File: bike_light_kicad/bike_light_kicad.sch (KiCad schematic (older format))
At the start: 58 parts, among them J1 12401832E402A, J2 AVR-ISP-6, SW1 SW_SPST, SW2 SW_SPST, U1 BQ29700, U2 bq21040, U3 CSD16406Q3, U4 CSD16406Q3, U5 ATtiny85-20SU, U6 LM2621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

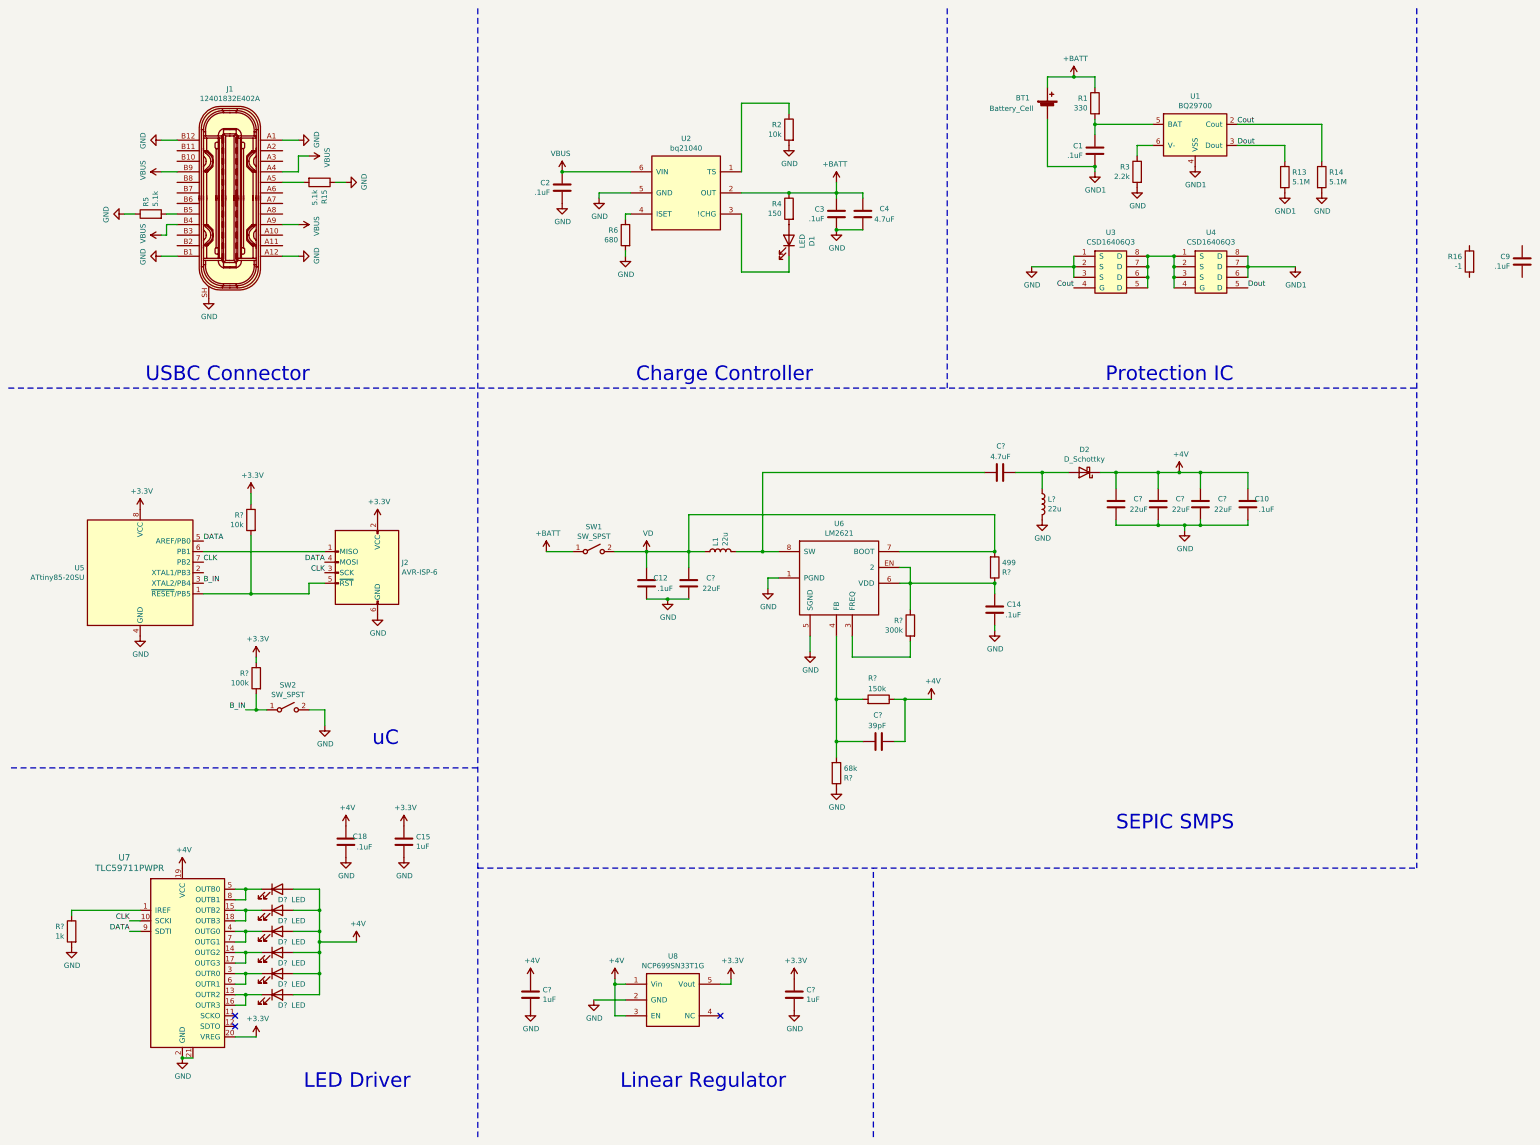
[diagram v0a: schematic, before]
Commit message: Footprints added, new manual lib
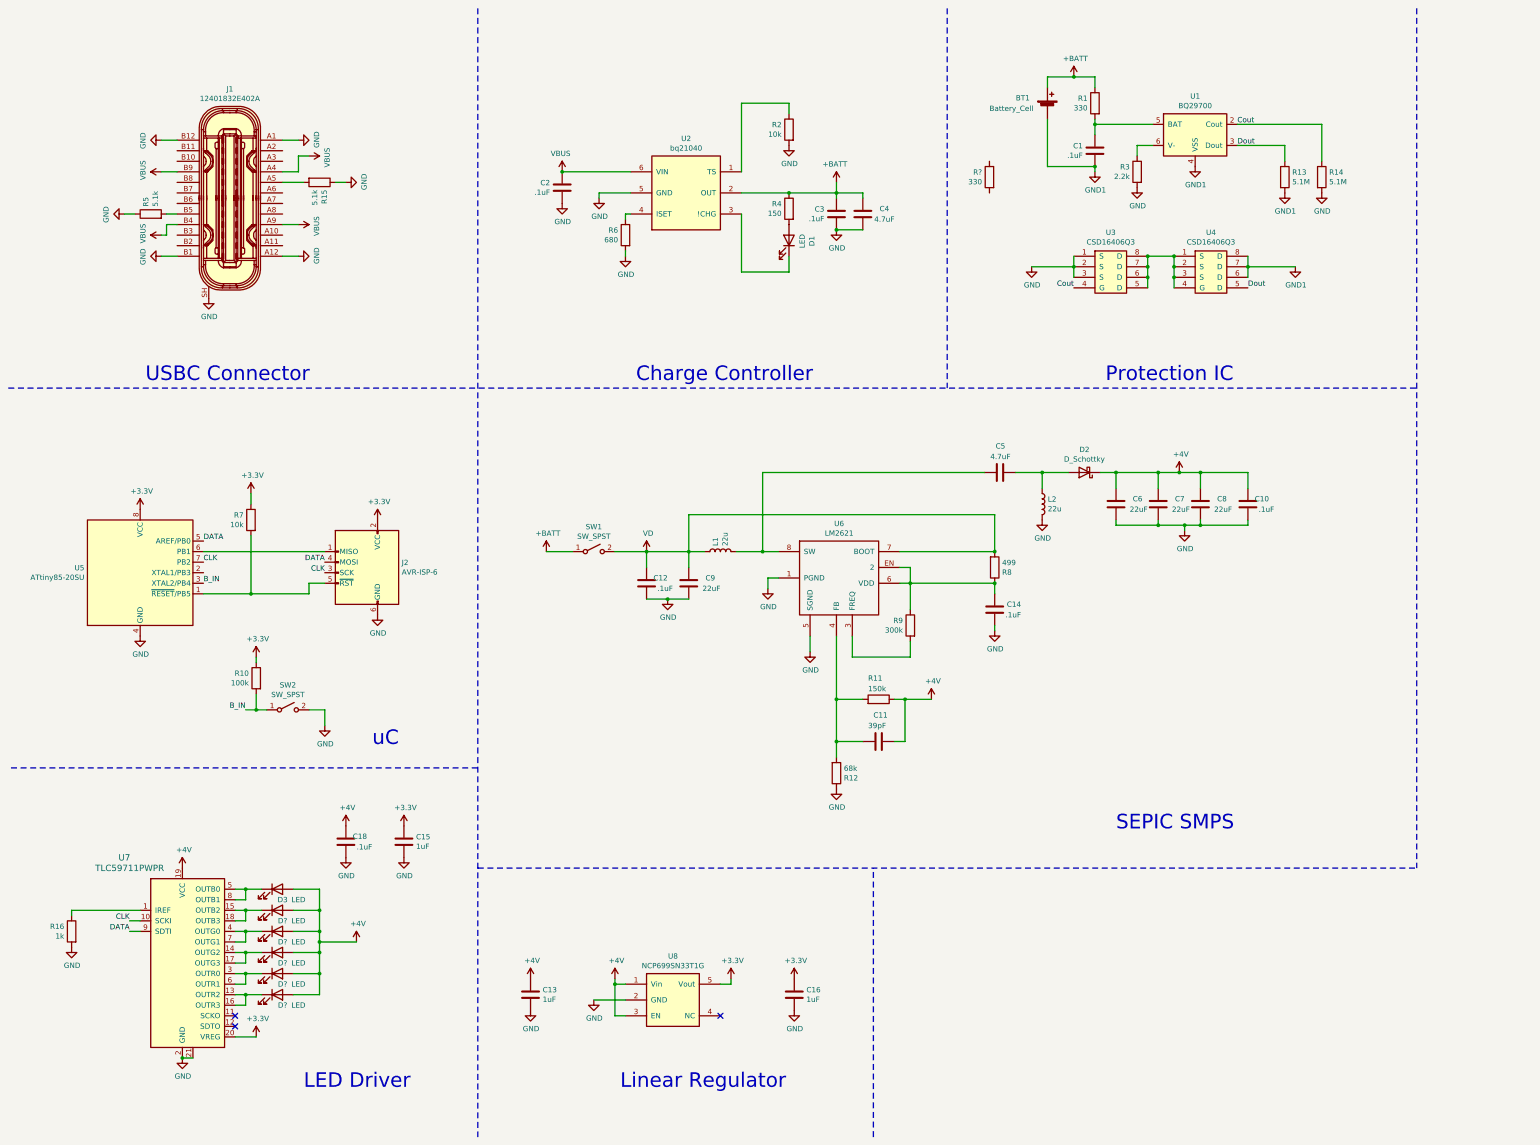
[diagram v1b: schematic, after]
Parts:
- removed C9: .1uF, Capacitors_SMD:C_0603, symbol Device:C
- removed D? (x5): LED, symbol Device:LED
- removed R16: -1, Resistors_SMD:R_0603, symbol Device:R
- added D? (x5): LED, Manual_Library:1510-2183-1-ND, symbol Device:LED
- added R?: 330, Resistors_SMD:R_0603, symbol Device:R
- BT1: footprint (none) -> Manual_Library:36-254-ND; Cell Case DPN (none) -> 36-254-ND; Digi-Key_PN (none) -> 1568-1488-ND; MPN (none) -> PRT-12895
- D1: footprint (none) -> LEDs:LED_0603
- D3: renamed from D?; footprint (none) -> Manual_Library:1510-2183-1-ND
- J2: footprint Connector_PinSocket_2.54mm:PinSocket_2x03_P2.54mm_Vertical -> Connectors:PINHEAD1-6; Digi-Key_PN (none) -> 1528-2946-ND; MPN (none) -> 4173
- L1: footprint (none) -> Manual_Library:SRU1038-220YCT-ND
- L2: renamed from L?; footprint (none) -> Manual_Library:SRU1038-220YCT-ND
- SW1: footprint (none) -> Manual_Library:CKC5106-ND; Digi-Key_PN (none) -> CKC5106-ND; MPN (none) -> L101011MS02Q
- U6: footprint Package_SO:VSSOP-8_3.0x3.0mm_P0.65mm -> Housings_SSOP:VSSOP-8_3.0x3.0mm_Pitch0.65mm
- gave numbers to parts that had none: 15
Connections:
- net +4V: now also D?.2 (A), D?.2 (A), D?.2 (A), D?.2 (A), D?.2 (A)
- net at U7.13 (OUTR2), U7.16 (OUTR3): now also D?.1 (K)
- net at U7.14 (OUTG2), U7.17 (OUTG3): now also D?.1 (K)
- net at U7.15 (OUTB2), U7.18 (OUTB3): now also D?.1 (K)
- net at U7.3 (OUTR0), U7.6 (OUTR1): now also D?.1 (K)
- net at U7.4 (OUTG0), U7.7 (OUTG1): now also D?.1 (K)

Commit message: Added components to .kicad_pcb file
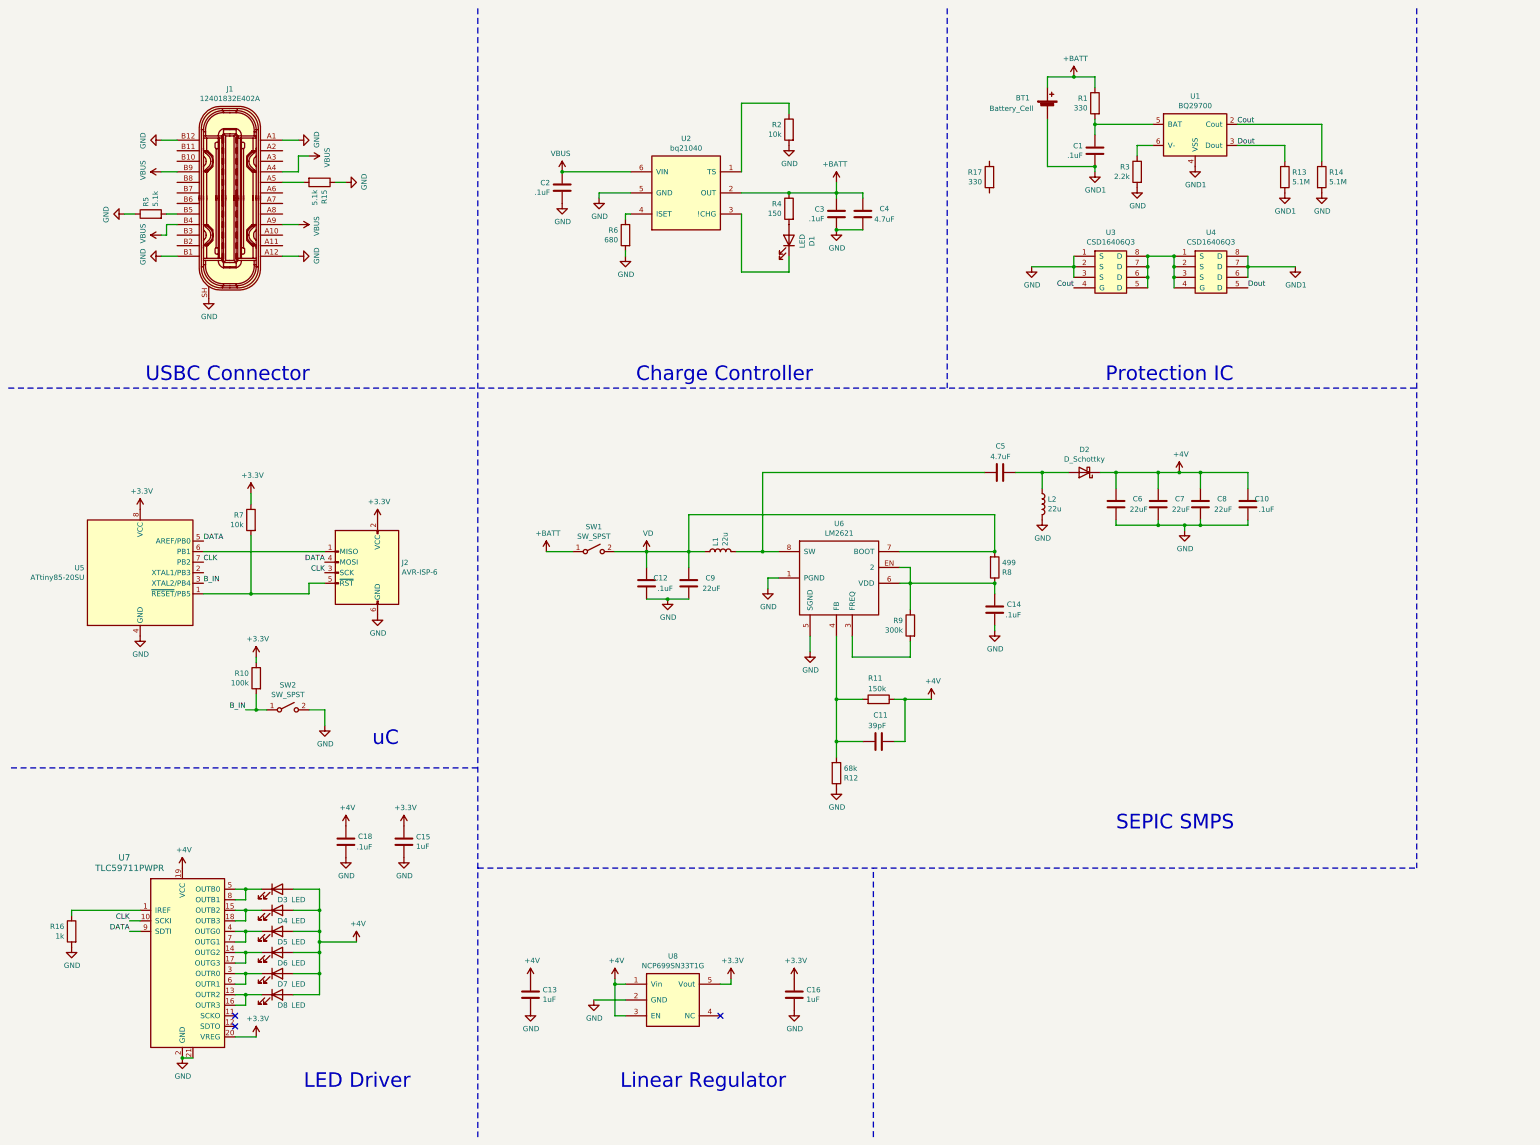
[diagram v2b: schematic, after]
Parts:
- C13, C15, C16, C18: footprint Capacitor_SMD:C_0603_1608Metric -> Capacitors_SMD:C_0603
- J1: footprint digikey-footprints:USB-C_Female_12401X -> digikey-footprints:USB_Type_C_Female__12401610E4_2A
- U1: footprint Package_SON:WSON-6_1.5x1.5mm_P0.5mm -> Housings_SON:WSON6_1.5x1.5mm_Pitch0.5mm
- U5: footprint Package_SO:SOIJ-8_5.3x5.3mm_P1.27mm -> Housings_SOIC:SOIJ-8_5.3x5.3mm_Pitch1.27mm
- U8: footprint Package_TO_SOT_SMD:SOT-23-5 -> TO_SOT_Packages_SMD:SOT-23-5
- gave numbers to parts that had none: 6
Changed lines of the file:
@@
 F 0 "U1" H 11750 2067 50  0000 C CNN
 F 1 "BQ29700" H 11750 1976 50  0000 C CNN
-F 2 "Package_SON:WSON-6_1.5x1.5mm_P0.5mm" H 11750 2050 50  0001 C CNN
+F 2 "Housings_SON:WSON6_1.5x1.5mm_Pitch0.5mm" H 11750 2050 50  0001 C CNN
 F 3 "http://www.ti.com/lit/ds/symlink/bq2970.pdf" H 11500 1900 50  0001 C CNN
 F 4 "296-43985-1-ND" H 11750 1700 50  0001 C CNN "Digi-Key_PN"
@@
 F 0 "J1" H 2600 3335 50  0000 C CNN
 F 1 "12401832E402A" H 2600 3244 50  0000 C CNN
-F 2 "digikey-footprints:USB-C_Female_12401X" H 2800 2500 60  0001 L CNN
+F 2 "digikey-footprints:USB_Type_C_Female__12401610E4_2A" H 2800 2500 60  0001 L CNN
 F 3 "https://media.digikey.com/pdf/Data%20Sheets/Amphenol%20PDFs/12401832E402A_Dwg_RevX1_04-25-17.pdf" H 2800 2600 60  0001 L CNN
 F 4 "12401832E402ACT-ND" H 2800 2700 60  0001 L CNN "Digi-Key_PN"
@@
 F 0 "U5" H 1221 5896 50  0000 R CNN
 F 1 "ATtiny85-20SU" H 1221 5805 50  0000 R CNN
-F 2 "Package_SO:SOIJ-8_5.3x5.3mm_P1.27mm" H 1750 5850 50  0001 C CIN
+F 2 "Housings_SOIC:SOIJ-8_5.3x5.3mm_Pitch1.27mm" H 1750 5850 50  0001 C CIN
 F 3 "http://ww1.microchip.com/downloads/en/DeviceDoc/atmel-2586-avr-8-bit-microcontroller-attiny25-attiny45-attiny85_datasheet.pdf" H 1750 5850 50  0001 C CNN
 F 4 "ATTINY85-20SURCT-ND" H 1750 5850 50  0001 C CNN "Digi-Key_PN"
@@
 F 0 "C15" H 4365 8446 50  0000 L CNN
 F 1 "1uF" H 4365 8355 50  0000 L CNN
-F 2 "Capacitor_SMD:C_0603_1608Metric" H 4288 8250 50  0001 C CNN
+F 2 "Capacitors_SMD:C_0603" H 4288 8250 50  0001 C CNN
 F 3 "" H 4250 8400 50  0001 C CNN
 F 4 "399-11136-1-ND" H 4250 8400 50  0001 C CNN "Digi-Key_PN"
@@
 F 0 "U8" H 6800 11015 50  0000 C CNN
 F 1 "NCP699SN33T1G" H 6800 10924 50  0000 C CNN
-F 2 "Package_TO_SOT_SMD:SOT-23-5" H 6800 10250 50  0001 C CNN
+F 2 "TO_SOT_Packages_SMD:SOT-23-5" H 6800 10250 50  0001 C CNN
 F 3 "" H 6800 10250 50  0001 C CNN
 F 4 "NCP699SN33T1GOSCT-ND" H 6800 10250 50  0001 C CNN "Digi-Key_PN"
@@
 U 1 1 5F6BDB4E
 P 3700 8400
-F 0 "C18" H 3500 8450 50  0000 L CNN
+F 0 "C18" H 3450 8450 50  0000 L CNN
 F 1 ".1uF" H 3450 8350 50  0000 L CNN
-F 2 "Capacitor_SMD:C_0603_1608Metric" H 3738 8250 50  0001 C CNN
+F 2 "Capacitors_SMD:C_0603" H 3738 8250 50  0001 C CNN
 F 3 "" H 3700 8400 50  0001 C CNN
 F 4 "399-1099-1-ND" H 3700 8400 50  0001 C CNN "Digi-Key_PN"
@@
 F 0 "C13" H 5565 9896 50  0000 L CNN
 F 1 "1uF" H 5565 9805 50  0000 L CNN
-F 2 "Capacitor_SMD:C_0603_1608Metric" H 5488 9700 50  0001 C CNN
+F 2 "Capacitors_SMD:C_0603" H 5488 9700 50  0001 C CNN
 F 3 "" H 5450 9850 50  0001 C CNN
 F 4 "399-11136-1-ND" H 5450 9850 50  0001 C CNN "Digi-Key_PN"
@@
 F 0 "C16" H 8065 9896 50  0000 L CNN
 F 1 "1uF" H 8065 9805 50  0000 L CNN
-F 2 "Capacitor_SMD:C_0603_1608Metric" H 7988 9700 50  0001 C CNN
+F 2 "Capacitors_SMD:C_0603" H 7988 9700 50  0001 C CNN
 F 3 "" H 7950 9850 50  0001 C CNN
 F 4 "399-11136-1-ND" H 7950 9850 50  0001 C CNN "Digi-Key_PN"
@@
 $EndComp
 $Comp
-L Device:R R?
+L Device:R R17
 U 1 1 5F620D0C
 P 9800 2100
-F 0 "R?" H 9870 2146 50  0000 L CNN
+F 0 "R17" H 9870 2146 50  0000 L CNN
 F 1 "330" H 9870 2055 50  0000 L CNN
 F 2 "Resistors_SMD:R_0603" V 9730 2100 50  0001 C CNN
@@
 $EndComp
 $Comp
-L Device:LED D?
+L Device:LED D4
 U 1 1 5F630C8F
 P 3050 9050
-F 0 "D?" H 3100 8950 50  0000 C CNN
+F 0 "D4" H 3100 8950 50  0000 C CNN
 F 1 "LED" H 3250 8950 50  0000 C CNN
 F 2 "Manual_Library:1510-2183-1-ND" H 3050 9050 50  0001 C CNN
@@
 $EndComp
 $Comp
-L Device:LED D?
+L Device:LED D5
 U 1 1 5F6316E2
 P 3050 9250
-F 0 "D?" H 3100 9150 50  0000 C CNN
+F 0 "D5" H 3100 9150 50  0000 C CNN
 F 1 "LED" H 3250 9150 50  0000 C CNN
 F 2 "Manual_Library:1510-2183-1-ND" H 3050 9250 50  0001 C CNN
@@
 $EndComp
 $Comp
-L Device:LED D?
+L Device:LED D6
 U 1 1 5F631A4E
 P 3050 9450
-F 0 "D?" H 3100 9350 50  0000 C CNN
+F 0 "D6" H 3100 9350 50  0000 C CNN
 F 1 "LED" H 3250 9350 50  0000 C CNN
 F 2 "Manual_Library:1510-2183-1-ND" H 3050 9450 50  0001 C CNN
@@
 $EndComp
 $Comp
-L Device:LED D?
+L Device:LED D7
 U 1 1 5F631E93
 P 3050 9650
-F 0 "D?" H 3100 9550 50  0000 C CNN
+F 0 "D7" H 3100 9550 50  0000 C CNN
 F 1 "LED" H 3250 9550 50  0000 C CNN
 F 2 "Manual_Library:1510-2183-1-ND" H 3050 9650 50  0001 C CNN
@@
 $EndComp
 $Comp
-L Device:LED D?
+L Device:LED D8
 U 1 1 5F6323EF
 P 3050 9850
-F 0 "D?" H 3100 9750 50  0000 C CNN
+F 0 "D8" H 3100 9750 50  0000 C CNN
 F 1 "LED" H 3250 9750 50  0000 C CNN
 F 2 "Manual_Library:1510-2183-1-ND" H 3050 9850 50  0001 C CNN
